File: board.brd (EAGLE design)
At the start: 160 x 100 mm, 6 parts

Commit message: minor updates
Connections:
- net GND: now also PORTD.7, PORTD.8
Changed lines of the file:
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@@
 <signal name="GND">
 <contactref element="U$1" pad="10"/>
+<contactref element="PORTD" pad="7"/>
+<contactref element="PORTD" pad="8"/>
+<contactref element="U$1" pad="10"/>
+<wire x1="46.99" y1="3.81" x2="79.28" y2="8.05" width="0" layer="19" extent="1-1"/>
+<wire x1="44.45" y1="3.81" x2="46.99" y2="3.81" width="0" layer="19" extent="1-1"/>
 </signal>
 <signal name="VDD">

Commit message: placing a stacking header so we can get reset and 3.3v from the xmega board
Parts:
- added PDI_STACK: AVR_SPI_PRG_6NS, SparkFun-Connectors:2X3-NS
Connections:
- new net PDI_DATA: PDI_STACK.1
- new net PDI_RESET/CLK: PDI_STACK.5
- new net VXMEGA: PDI_STACK.2
- net GND: now also PDI_STACK.6
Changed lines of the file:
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@@
 <element name="U$1" library="SparkFun-RF" package="XBEE-SILK" value="XBEE-1B2" x="81.28" y="19.05" rot="R90"/>
 <element name="PORTA" library="SparkFun-Connectors" package="1X08" value="" x="36.83" y="24.13" locked="yes" rot="R180"/>
-<element name="PORTC" library="SparkFun-Connectors" package="1X08" value="" x="8.89" y="3.81" locked="yes"/>
+<element name="PORTC" library="SparkFun-Connectors" package="1X08" value="" x="8.89" y="3.81" locked="yes" smashed="yes">
+<attribute name="NAME" x="17.7038" y="5.6388" size="1.27" layer="25" ratio="10"/>
+<attribute name="VALUE" x="7.62" y="0.635" size="1.27" layer="27"/>
+</element>
 <element name="PORTD" library="SparkFun-Connectors" package="1X08" value="" x="29.21" y="3.81" locked="yes"/>
 <element name="PORTB" library="SparkFun-Connectors" package="1X04" value="" x="16.51" y="24.13" locked="yes" rot="R180"/>
 <element name="PORTE" library="SparkFun-Connectors" package="1X04" value="" x="46.99" y="24.13" locked="yes" rot="R180"/>
+<element name="PDI_STACK" library="SparkFun-Connectors" package="2X3-NS" value="AVR_SPI_PRG_6NS" x="10.795" y="8.89" smashed="yes" rot="R90">
+<attribute name="NAME" x="15.24" y="6.35" size="1.27" layer="25" ratio="10" rot="R90"/>
+</element>
 </elements>
 <signals>
@@
 <contactref element="PORTD" pad="8"/>
 <contactref element="U$1" pad="10"/>
+<contactref element="PDI_STACK" pad="6"/>
 <wire x1="46.99" y1="3.81" x2="79.28" y2="8.05" width="0" layer="19" extent="1-1"/>
 <wire x1="44.45" y1="3.81" x2="46.99" y2="3.81" width="0" layer="19" extent="1-1"/>
+<wire x1="9.525" y1="11.43" x2="44.45" y2="3.81" width="0" layer="19" extent="1-1"/>
 </signal>
 <signal name="VDD">
 <contactref element="U$1" pad="1"/>
 </signal>
+<signal name="PDI_DATA">
+<contactref element="PDI_STACK" pad="1"/>
+</signal>
+<signal name="PDI_RESET/CLK">
+<contactref element="PDI_STACK" pad="5"/>
+</signal>
+<signal name="VXMEGA">
+<contactref element="PDI_STACK" pad="2"/>
+</signal>
 </signals>

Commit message: stack the power connector too and mark out the 50x50mm board area for cheapest chinese boards
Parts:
- removed U$1: XBEE-1B2, SparkFun-RF:XBEE-SILK
- added PWR_STACK: (no value), SparkFun-Connectors:1X03
- added XBEE: XBEE-1B2, SparkFun-RF:XBEE-SILK
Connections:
- new net VBAT: PWR_STACK.1
- net GND: now also PWR_STACK.2, XBEE.10; no longer U$1.10
- net VDD: now also XBEE.1; no longer U$1.1
- net VXMEGA: now also PWR_STACK.3
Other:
- board size 160 x 100 mm -> 50 x 50 mm
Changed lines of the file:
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@@
 <setting verticaltext="up"/>
 </settings>
-<grid distance="0.05" unitdist="inch" unit="mil" style="lines" multiple="1" display="yes" altdistance="0.025" altunitdist="inch" altunit="mil"/>
+<grid distance="0.05" unitdist="inch" unit="mm" style="lines" multiple="1" display="yes" altdistance="0.025" altunitdist="inch" altunit="mm"/>
 <layers>
 <layer number="1" name="Top" color="4" fill="1" visible="yes" active="yes"/>
@@
 <board>
 <plain>
-<wire x1="0" y1="0" x2="160" y2="0" width="0" layer="20"/>
-<wire x1="160" y1="0" x2="160" y2="100" width="0" layer="20"/>
-<wire x1="160" y1="100" x2="0" y2="100" width="0" layer="20"/>
-<wire x1="0" y1="100" x2="0" y2="0" width="0" layer="20"/>
+<wire x1="0" y1="0" x2="50" y2="0" width="0" layer="20"/>
+<wire x1="50" y1="0" x2="50" y2="50" width="0" layer="20"/>
+<wire x1="50" y1="50" x2="0" y2="50" width="0" layer="20"/>
+<wire x1="0" y1="50" x2="0" y2="0" width="0" layer="20"/>
 </plain>
 <attributes>
@@
 </autorouter>
 <elements>
-<element name="U$1" library="SparkFun-RF" package="XBEE-SILK" value="XBEE-1B2" x="81.28" y="19.05" rot="R90"/>
+<element name="XBEE" library="SparkFun-RF" package="XBEE-SILK" value="XBEE-1B2" x="27.94" y="38.1" rot="R90"/>
 <element name="PORTA" library="SparkFun-Connectors" package="1X08" value="" x="36.83" y="24.13" locked="yes" rot="R180"/>
 <element name="PORTC" library="SparkFun-Connectors" package="1X08" value="" x="8.89" y="3.81" locked="yes" smashed="yes">
@@
 <element name="PORTB" library="SparkFun-Connectors" package="1X04" value="" x="16.51" y="24.13" locked="yes" rot="R180"/>
 <element name="PORTE" library="SparkFun-Connectors" package="1X04" value="" x="46.99" y="24.13" locked="yes" rot="R180"/>
-<element name="PDI_STACK" library="SparkFun-Connectors" package="2X3-NS" value="AVR_SPI_PRG_6NS" x="10.795" y="8.89" smashed="yes" rot="R90">
+<element name="PDI_STACK" library="SparkFun-Connectors" package="2X3-NS" value="AVR_SPI_PRG_6NS" x="10.795" y="8.89" locked="yes" smashed="yes" rot="R90">
 <attribute name="NAME" x="15.24" y="6.35" size="1.27" layer="25" ratio="10" rot="R90"/>
 </element>
+<element name="PWR_STACK" library="SparkFun-Connectors" package="1X03" value="" x="5.08" y="6.35" locked="yes" rot="R90"/>
 </elements>
 <signals>
 <signal name="GND">
-<contactref element="U$1" pad="10"/>
+<contactref element="XBEE" pad="10"/>
 <contactref element="PORTD" pad="7"/>
 <contactref element="PORTD" pad="8"/>
-<contactref element="U$1" pad="10"/>
+<contactref element="XBEE" pad="10"/>
 <contactref element="PDI_STACK" pad="6"/>
-<wire x1="46.99" y1="3.81" x2="79.28" y2="8.05" width="0" layer="19" extent="1-1"/>
+<contactref element="PWR_STACK" pad="2"/>
+<wire x1="46.99" y1="3.81" x2="25.94" y2="27.1" width="0" layer="19" extent="1-1"/>
 <wire x1="44.45" y1="3.81" x2="46.99" y2="3.81" width="0" layer="19" extent="1-1"/>
 <wire x1="9.525" y1="11.43" x2="44.45" y2="3.81" width="0" layer="19" extent="1-1"/>
+<wire x1="5.08" y1="8.89" x2="9.525" y2="11.43" width="0" layer="19" extent="1-1"/>
 </signal>
 <signal name="VDD">
-<contactref element="U$1" pad="1"/>
+<contactref element="XBEE" pad="1"/>
 </signal>
 <signal name="PDI_DATA">
@@
 <signal name="VXMEGA">
 <contactref element="PDI_STACK" pad="2"/>
+<contactref element="PWR_STACK" pad="3"/>
+<wire x1="5.08" y1="11.43" x2="9.525" y2="6.35" width="0" layer="19" extent="1-1"/>
+</signal>
+<signal name="VBAT">
+<contactref element="PWR_STACK" pad="1"/>
 </signal>
 </signals>

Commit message: use the stub portd for rx/tx in case someone is using the rtc xtal on porte
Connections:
- new net XMEGA_RX: PORTD.3, XBEE.2
- new net XMEGA_TX: PORTD.4, XBEE.3
- net PDI_RESET/CLK: now also XBEE.9
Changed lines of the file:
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@@
 <signal name="PDI_RESET/CLK">
 <contactref element="PDI_STACK" pad="5"/>
+<contactref element="XBEE" pad="9"/>
+<wire x1="12.065" y1="11.43" x2="23.94" y2="27.1" width="0" layer="19" extent="1-1"/>
 </signal>
 <signal name="VXMEGA">
@@
 <contactref element="PWR_STACK" pad="1"/>
 </signal>
+<signal name="XMEGA_RX">
+<contactref element="PORTD" pad="3"/>
+<contactref element="XBEE" pad="2"/>
+<wire x1="9.94" y1="27.1" x2="34.29" y2="3.81" width="0" layer="19" extent="1-1"/>
+</signal>
+<signal name="XMEGA_TX">
+<contactref element="PORTD" pad="4"/>
+<contactref element="XBEE" pad="3"/>
+<wire x1="11.94" y1="27.1" x2="36.83" y2="3.81" width="0" layer="19" extent="1-1"/>
+</signal>
 </signals>

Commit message: use the stub portd for rx/tx in case someone is using the rtc xtal on porte
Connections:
- new net SCL: PORTE.2
- new net SDA: PORTE.1
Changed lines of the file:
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@@
 <wire x1="11.94" y1="27.1" x2="36.83" y2="3.81" width="0" layer="19" extent="1-1"/>
+</signal>
+<signal name="SDA">
+<contactref element="PORTE" pad="1"/>
+</signal>
+<signal name="SCL">
+<contactref element="PORTE" pad="2"/>
 </signal>
 </signals>

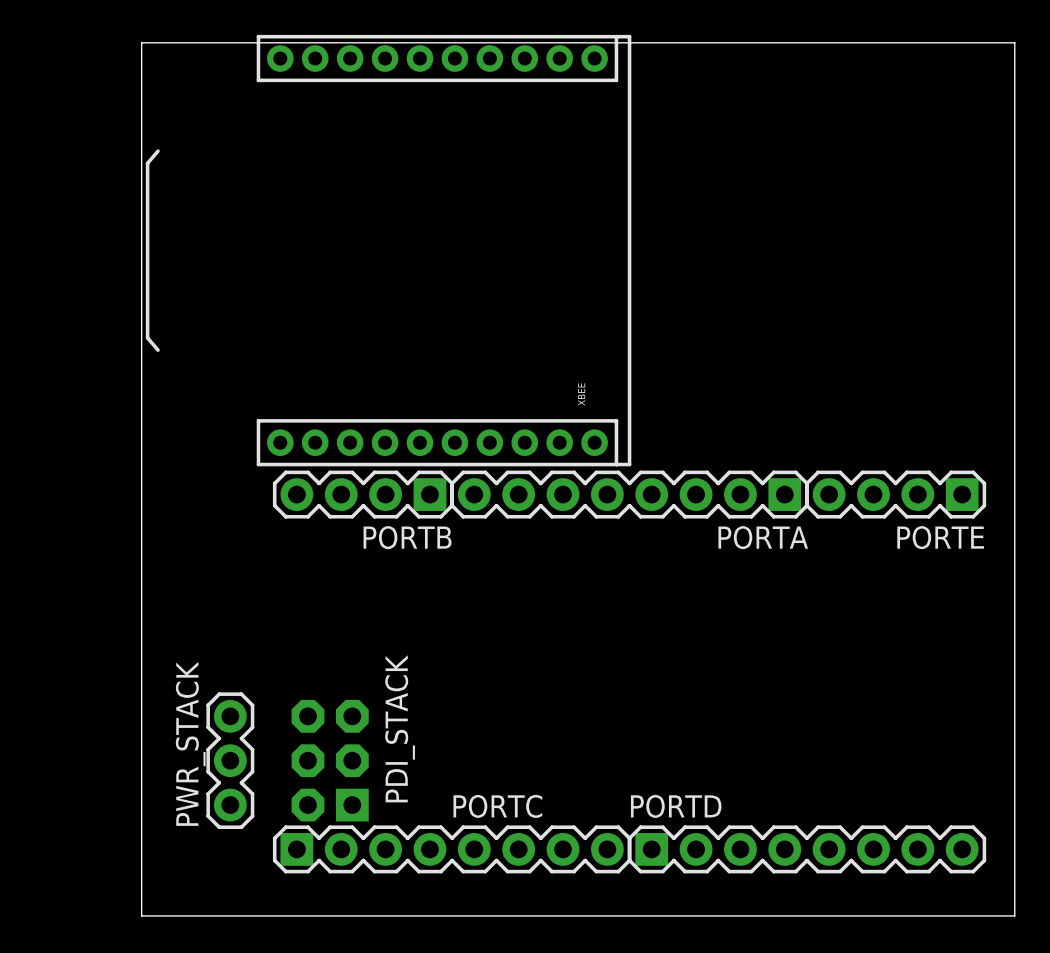
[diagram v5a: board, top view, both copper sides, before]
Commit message: reposition the xmega stacking headers, move the xbee breakout to top-left corner
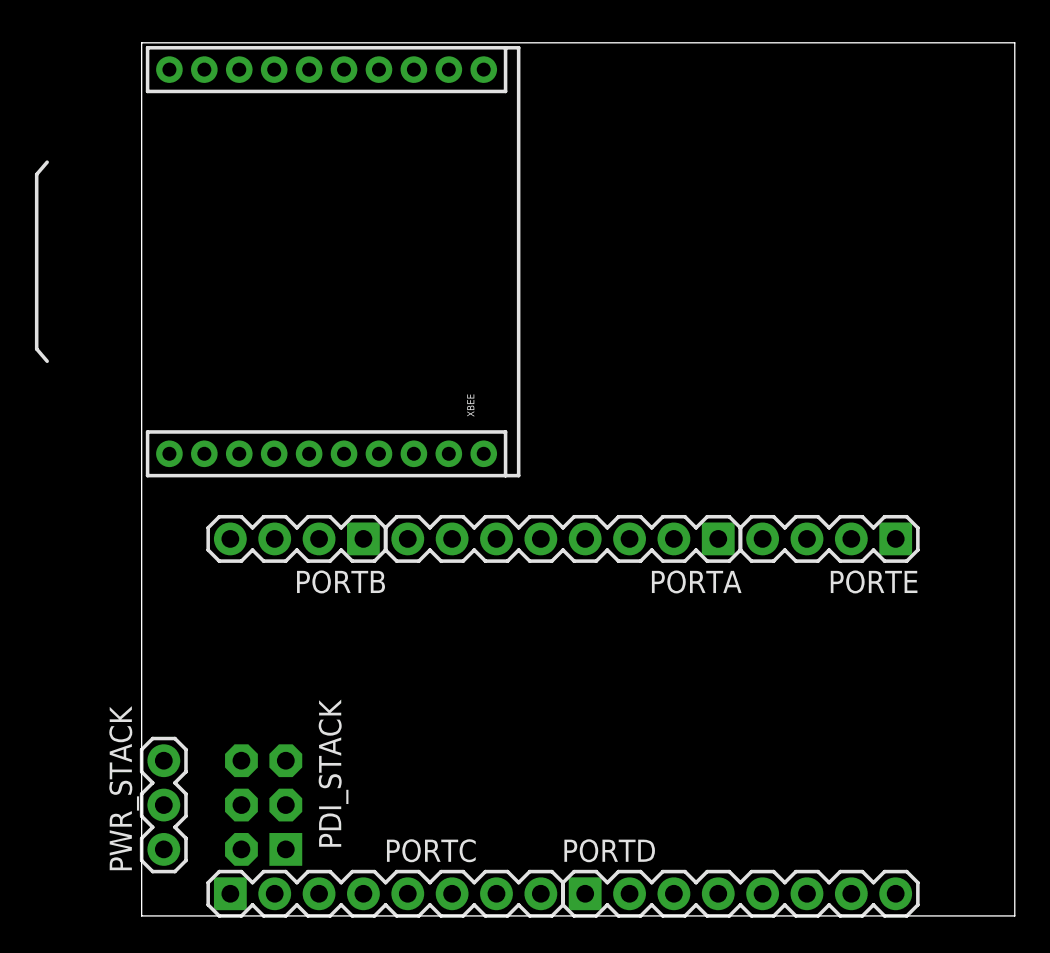
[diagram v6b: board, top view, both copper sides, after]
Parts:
- moved XBEE 6.38 mm to (21.6, 37.5)
- moved PORTB 4.58 mm to (12.7, 21.6)
- moved PORTD 4.58 mm to (25.4, 1.27)
- moved PORTE 4.58 mm to (43.2, 21.6)
- moved PDI_STACK 4.58 mm to (6.99, 6.35)
- moved PORTC 4.58 mm to (5.08, 1.27)
- moved PWR_STACK 4.58 mm to (1.27, 3.81)
- moved PORTA 4.58 mm to (33.0, 21.6)
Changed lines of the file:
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@@
 <setting verticaltext="up"/>
 </settings>
-<grid distance="0.05" unitdist="inch" unit="mm" style="lines" multiple="1" display="yes" altdistance="0.025" altunitdist="inch" altunit="mm"/>
+<grid distance="0.05" unitdist="inch" unit="mil" style="lines" multiple="1" display="yes" altdistance="0.025" altunitdist="inch" altunit="mil"/>
 <layers>
 <layer number="1" name="Top" color="4" fill="1" visible="yes" active="yes"/>
@@
 </autorouter>
 <elements>
-<element name="XBEE" library="SparkFun-RF" package="XBEE-SILK" value="XBEE-1B2" x="27.94" y="38.1" rot="R90"/>
-<element name="PORTA" library="SparkFun-Connectors" package="1X08" value="" x="36.83" y="24.13" locked="yes" rot="R180"/>
-<element name="PORTC" library="SparkFun-Connectors" package="1X08" value="" x="8.89" y="3.81" locked="yes" smashed="yes">
-<attribute name="NAME" x="17.7038" y="5.6388" size="1.27" layer="25" ratio="10"/>
-<attribute name="VALUE" x="7.62" y="0.635" size="1.27" layer="27"/>
+<element name="XBEE" library="SparkFun-RF" package="XBEE-SILK" value="XBEE-1B2" x="21.59" y="37.465" rot="R90"/>
+<element name="PORTA" library="SparkFun-Connectors" package="1X08" value="" x="33.02" y="21.59" locked="yes" rot="R180"/>
+<element name="PORTC" library="SparkFun-Connectors" package="1X08" value="" x="5.08" y="1.27" locked="yes" smashed="yes">
+<attribute name="NAME" x="13.8938" y="3.0988" size="1.27" layer="25" ratio="10"/>
+<attribute name="VALUE" x="3.81" y="-1.905" size="1.27" layer="27"/>
 </element>
-<element name="PORTD" library="SparkFun-Connectors" package="1X08" value="" x="29.21" y="3.81" locked="yes"/>
-<element name="PORTB" library="SparkFun-Connectors" package="1X04" value="" x="16.51" y="24.13" locked="yes" rot="R180"/>
-<element name="PORTE" library="SparkFun-Connectors" package="1X04" value="" x="46.99" y="24.13" locked="yes" rot="R180"/>
-<element name="PDI_STACK" library="SparkFun-Connectors" package="2X3-NS" value="AVR_SPI_PRG_6NS" x="10.795" y="8.89" locked="yes" smashed="yes" rot="R90">
-<attribute name="NAME" x="15.24" y="6.35" size="1.27" layer="25" ratio="10" rot="R90"/>
+<element name="PORTD" library="SparkFun-Connectors" package="1X08" value="" x="25.4" y="1.27" locked="yes"/>
+<element name="PORTB" library="SparkFun-Connectors" package="1X04" value="" x="12.7" y="21.59" locked="yes" rot="R180"/>
+<element name="PORTE" library="SparkFun-Connectors" package="1X04" value="" x="43.18" y="21.59" locked="yes" rot="R180"/>
+<element name="PDI_STACK" library="SparkFun-Connectors" package="2X3-NS" value="AVR_SPI_PRG_6NS" x="6.985" y="6.35" locked="yes" smashed="yes" rot="R90">
+<attribute name="NAME" x="11.43" y="3.81" size="1.27" layer="25" ratio="10" rot="R90"/>
 </element>
-<element name="PWR_STACK" library="SparkFun-Connectors" package="1X03" value="" x="5.08" y="6.35" locked="yes" rot="R90"/>
+<element name="PWR_STACK" library="SparkFun-Connectors" package="1X03" value="" x="1.27" y="3.81" locked="yes" rot="R90"/>
 </elements>
 <signals>
@@
 <contactref element="PDI_STACK" pad="6"/>
 <contactref element="PWR_STACK" pad="2"/>
-<wire x1="46.99" y1="3.81" x2="25.94" y2="27.1" width="0" layer="19" extent="1-1"/>
-<wire x1="44.45" y1="3.81" x2="46.99" y2="3.81" width="0" layer="19" extent="1-1"/>
-<wire x1="9.525" y1="11.43" x2="44.45" y2="3.81" width="0" layer="19" extent="1-1"/>
-<wire x1="5.08" y1="8.89" x2="9.525" y2="11.43" width="0" layer="19" extent="1-1"/>
+<wire x1="43.18" y1="1.27" x2="19.59" y2="26.465" width="0" layer="19" extent="1-1"/>
+<wire x1="40.64" y1="1.27" x2="43.18" y2="1.27" width="0" layer="19" extent="1-1"/>
+<wire x1="5.715" y1="8.89" x2="40.64" y2="1.27" width="0" layer="19" extent="1-1"/>
+<wire x1="1.27" y1="6.35" x2="5.715" y2="8.89" width="0" layer="19" extent="1-1"/>
 </signal>
 <signal name="VDD">
@@
 <contactref element="PDI_STACK" pad="5"/>
 <contactref element="XBEE" pad="9"/>
-<wire x1="12.065" y1="11.43" x2="23.94" y2="27.1" width="0" layer="19" extent="1-1"/>
+<wire x1="8.255" y1="8.89" x2="17.59" y2="26.465" width="0" layer="19" extent="1-1"/>
 </signal>
 <signal name="VXMEGA">
 <contactref element="PDI_STACK" pad="2"/>
 <contactref element="PWR_STACK" pad="3"/>
-<wire x1="5.08" y1="11.43" x2="9.525" y2="6.35" width="0" layer="19" extent="1-1"/>
+<wire x1="1.27" y1="8.89" x2="5.715" y2="3.81" width="0" layer="19" extent="1-1"/>
 </signal>
 <signal name="VBAT">
@@
 <contactref element="PORTD" pad="3"/>
 <contactref element="XBEE" pad="2"/>
-<wire x1="9.94" y1="27.1" x2="34.29" y2="3.81" width="0" layer="19" extent="1-1"/>
+<wire x1="3.59" y1="26.465" x2="30.48" y2="1.27" width="0" layer="19" extent="1-1"/>
 </signal>
 <signal name="XMEGA_TX">
 <contactref element="PORTD" pad="4"/>
 <contactref element="XBEE" pad="3"/>
-<wire x1="11.94" y1="27.1" x2="36.83" y2="3.81" width="0" layer="19" extent="1-1"/>
+<wire x1="5.59" y1="26.465" x2="33.02" y2="1.27" width="0" layer="19" extent="1-1"/>
 </signal>
 <signal name="SDA">

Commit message: noted the second UART
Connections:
- net VBAT renamed VXMEGA_USB
- net XMEGA_RX renamed XMEGA_RX0
- net XMEGA_TX renamed XMEGA_TX0
- new net XMEGA_RX1: PORTC.7
- new net XMEGA_TX1: PORTC.8
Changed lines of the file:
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@@
 <wire x1="1.27" y1="8.89" x2="5.715" y2="3.81" width="0" layer="19" extent="1-1"/>
 </signal>
-<signal name="VBAT">
-<contactref element="PWR_STACK" pad="1"/>
-</signal>
-<signal name="XMEGA_RX">
+<signal name="XMEGA_RX0">
 <contactref element="PORTD" pad="3"/>
 <contactref element="XBEE" pad="2"/>
 <wire x1="3.59" y1="26.465" x2="30.48" y2="1.27" width="0" layer="19" extent="1-1"/>
 </signal>
-<signal name="XMEGA_TX">
+<signal name="XMEGA_TX0">
 <contactref element="PORTD" pad="4"/>
 <contactref element="XBEE" pad="3"/>
@@
 <contactref element="PORTE" pad="2"/>
 </signal>
+<signal name="VXMEGA_USB">
+<contactref element="PWR_STACK" pad="1"/>
+</signal>
+<signal name="XMEGA_TX1">
+<contactref element="PORTC" pad="8"/>
+</signal>
+<signal name="XMEGA_RX1">
+<contactref element="PORTC" pad="7"/>
+</signal>
 </signals>
